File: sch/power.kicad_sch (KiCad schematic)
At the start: 17 parts, among them U6 MAX811MEUS-T

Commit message: Gerber Plots
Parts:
- C1, C14, C5: value (none) -> 10uF; footprint (none) -> Capacitor_SMD:C_0805_2012Metric
- C17, C19, C6: value (none) -> 1uF
- C20, C7, C8: value (none) -> 100nF
- D1: value (none) -> LED; footprint (none) -> LED_SMD:LED_0805_2012Metric
- R29: value (none) -> 4K7; footprint (none) -> Resistor_SMD:R_0805_2012Metric
- REG1: value (none) -> NCP1117ST50T3G; footprint (none) -> Package_TO_SOT_SMD:SOT-223-3_TabPin2
- REG2, REG3: value (none) -> NCP1117ST33T3G; footprint (none) -> Package_TO_SOT_SMD:SOT-223-3_TabPin2
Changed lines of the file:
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@@
       (effects (font (size 1.27 1.27)) hide)
     )
-    (property "Value" "" (id 1) (at 86.995 38.1 0))
+    (property "Value" "GND" (id 1) (at 86.995 38.1 0))
     (property "Footprint" "" (id 2) (at 86.995 33.655 0)
       (effects (font (size 1.27 1.27)) hide)
@@
       (effects (font (size 1.27 1.27)) (justify left))
     )
-    (property "Value" "" (id 1) (at 73.66 63.5 0)
-      (effects (font (size 1.27 1.27)) (justify right))
-    )
-    (property "Footprint" "" (id 2) (at 76.2 62.23 0)
+    (property "Value" "10uF" (id 1) (at 73.66 63.5 0)
+      (effects (font (size 1.27 1.27)) (justify right))
+    )
+    (property "Footprint" "Capacitor_SMD:C_0805_2012Metric" (id 2) (at 76.2 62.23 0)
       (effects (font (size 1.27 1.27)) hide)
     )
@@
       (effects (font (size 1.27 1.27)) (justify left))
     )
-    (property "Value" "" (id 1) (at 73.66 139.7 0)
-      (effects (font (size 1.27 1.27)) (justify right))
-    )
-    (property "Footprint" "" (id 2) (at 76.2 138.43 0)
+    (property "Value" "10uF" (id 1) (at 73.66 139.7 0)
+      (effects (font (size 1.27 1.27)) (justify right))
+    )
+    (property "Footprint" "Capacitor_SMD:C_0805_2012Metric" (id 2) (at 76.2 138.43 0)
       (effects (font (size 1.27 1.27)) hide)
     )
@@
     (in_bom yes) (on_board yes) (fields_autoplaced)
     (property "Reference" "REG1" (id 0) (at 90.17 49.53 0))
-    (property "Value" "" (id 1) (at 90.17 52.07 0))
-    (property "Footprint" "" (id 2) (at 90.17 52.07 0)
+    (property "Value" "NCP1117ST50T3G" (id 1) (at 90.17 52.07 0))
+    (property "Footprint" "Package_TO_SOT_SMD:SOT-223-3_TabPin2" (id 2) (at 90.17 52.07 0)
       (effects (font (size 1.27 1.27)) hide)
     )
@@
     (in_bom yes) (on_board yes) (fields_autoplaced)
     (property "Reference" "REG2" (id 0) (at 90.17 87.63 0))
-    (property "Value" "" (id 1) (at 90.17 90.17 0))
-    (property "Footprint" "" (id 2) (at 90.17 90.17 0)
+    (property "Value" "NCP1117ST33T3G" (id 1) (at 90.17 90.17 0))
+    (property "Footprint" "Package_TO_SOT_SMD:SOT-223-3_TabPin2" (id 2) (at 90.17 90.17 0)
       (effects (font (size 1.27 1.27)) hide)
     )
@@
       (effects (font (size 1.27 1.27)) (justify left))
     )
-    (property "Value" "" (id 1) (at 113.665 101.6 0)
+    (property "Value" "1uF" (id 1) (at 113.665 101.6 0)
       (effects (font (size 1.27 1.27)) (justify right))
     )
@@
       (effects (font (size 1.27 1.27)) (justify left))
     )
-    (property "Value" "" (id 1) (at 123.825 101.6 0)
+    (property "Value" "100nF" (id 1) (at 123.825 101.6 0)
       (effects (font (size 1.27 1.27)) (justify right))
     )
@@
       (effects (font (size 1.27 1.27)) (justify left))
     )
-    (property "Value" "" (id 1) (at 113.665 139.7 0)
+    (property "Value" "1uF" (id 1) (at 113.665 139.7 0)
       (effects (font (size 1.27 1.27)) (justify right))
     )
@@
     (in_bom yes) (on_board yes)
     (property "Reference" "D1" (id 0) (at 71.12 27.305 0))
-    (property "Value" "" (id 1) (at 71.12 29.845 0))
-    (property "Footprint" "" (id 2) (at 71.12 33.655 0)
+    (property "Value" "LED" (id 1) (at 71.12 29.845 0))
+    (property "Footprint" "LED_SMD:LED_0805_2012Metric" (id 2) (at 71.12 33.655 0)
       (effects (font (size 1.27 1.27)) hide)
     )
@@
     (in_bom yes) (on_board yes) (fields_autoplaced)
     (property "Reference" "R29" (id 0) (at 78.74 27.94 90))
-    (property "Value" "" (id 1) (at 78.74 30.48 90))
-    (property "Footprint" "" (id 2) (at 78.74 35.433 90)
+    (property "Value" "4K7" (id 1) (at 78.74 30.48 90))
+    (property "Footprint" "Resistor_SMD:R_0805_2012Metric" (id 2) (at 78.74 35.433 90)
       (effects (font (size 1.27 1.27)) hide)
     )
@@
     (in_bom yes) (on_board yes) (fields_autoplaced)
     (property "Reference" "REG3" (id 0) (at 90.17 125.73 0))
-    (property "Value" "" (id 1) (at 90.17 128.27 0))
-    (property "Footprint" "" (id 2) (at 90.17 128.27 0)
+    (property "Value" "NCP1117ST33T3G" (id 1) (at 90.17 128.27 0))
+    (property "Footprint" "Package_TO_SOT_SMD:SOT-223-3_TabPin2" (id 2) (at 90.17 128.27 0)
       (effects (font (size 1.27 1.27)) hide)
     )
@@
       (effects (font (size 1.27 1.27)) (justify left))
     )
-    (property "Value" "" (id 1) (at 73.66 101.6 0)
-      (effects (font (size 1.27 1.27)) (justify right))
-    )
-    (property "Footprint" "" (id 2) (at 76.2 100.33 0)
+    (property "Value" "10uF" (id 1) (at 73.66 101.6 0)
+      (effects (font (size 1.27 1.27)) (justify right))
+    )
+    (property "Footprint" "Capacitor_SMD:C_0805_2012Metric" (id 2) (at 76.2 100.33 0)
       (effects (font (size 1.27 1.27)) hide)
     )
@@
       (effects (font (size 1.27 1.27)) (justify left))
     )
-    (property "Value" "" (id 1) (at 123.825 63.5 0)
+    (property "Value" "100nF" (id 1) (at 123.825 63.5 0)
       (effects (font (size 1.27 1.27)) (justify right))
     )
@@
       (effects (font (size 1.27 1.27)) (justify left))
     )
-    (property "Value" "" (id 1) (at 123.825 139.7 0)
+    (property "Value" "100nF" (id 1) (at 123.825 139.7 0)
       (effects (font (size 1.27 1.27)) (justify right))
     )
@@
       (effects (font (size 1.27 1.27)) (justify left))
     )
-    (property "Value" "" (id 1) (at 113.665 63.5 0)
-      (effects (font (size 1.27 1.27)) (justify right))
-    )
+    (property "Value" "1uF" (id 1) (at 113.665 63.5 0)
+      (effects (font (size 1.27 1.27)) (justify right))
+    )

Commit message: some docs
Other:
- note added: "Power Delivery"
- note added: "Power Indicator"
- moved on the sheet: C1, C17, C5, C6, C7, C8, REG1, REG2

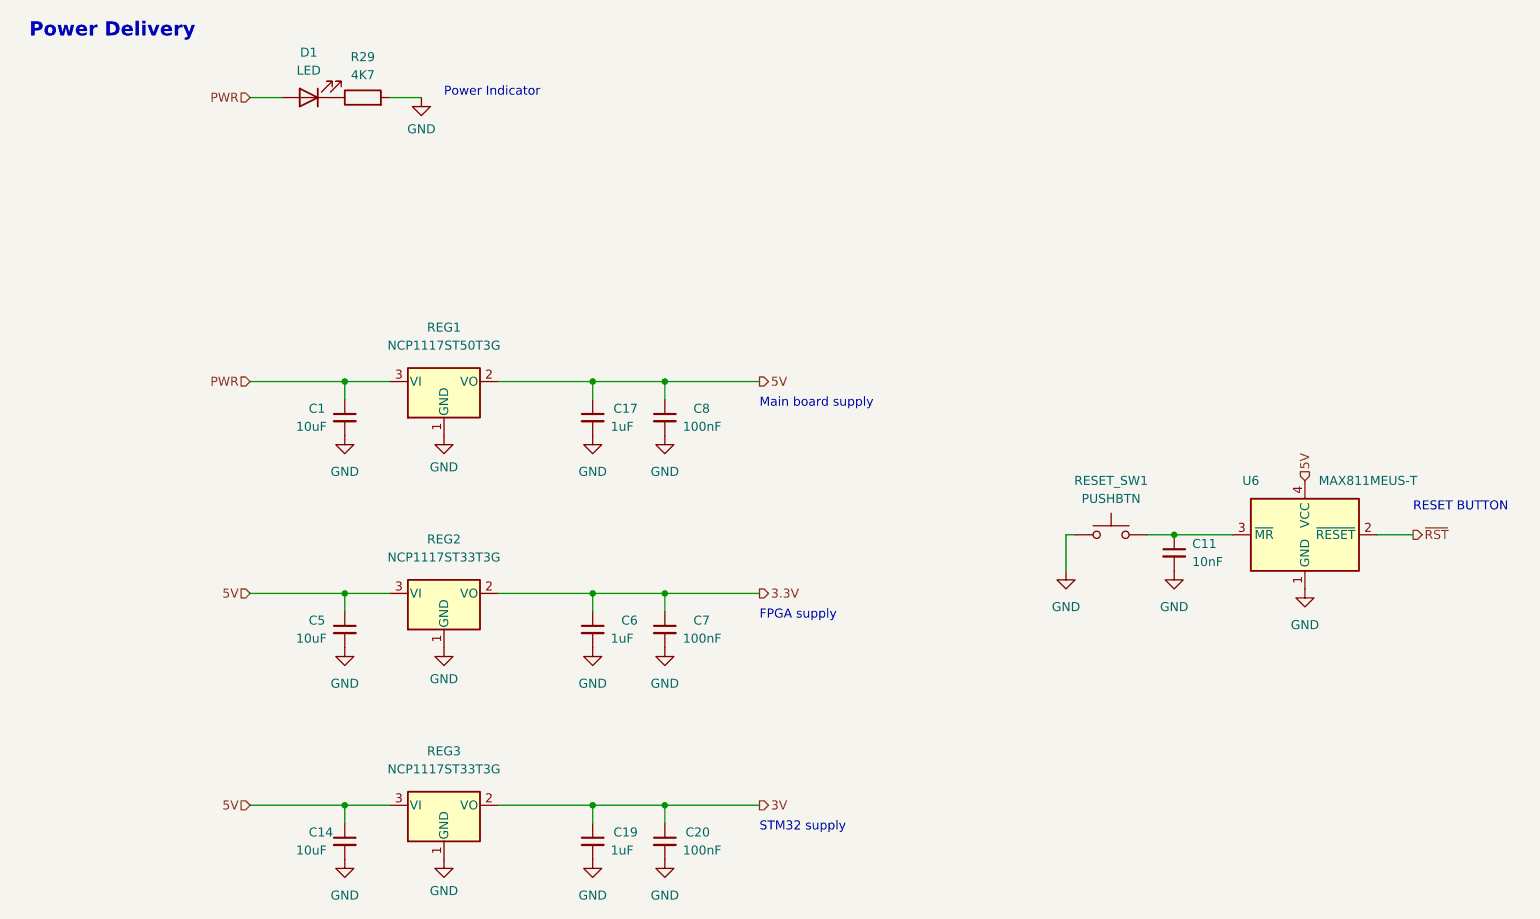
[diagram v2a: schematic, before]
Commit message: update schematic
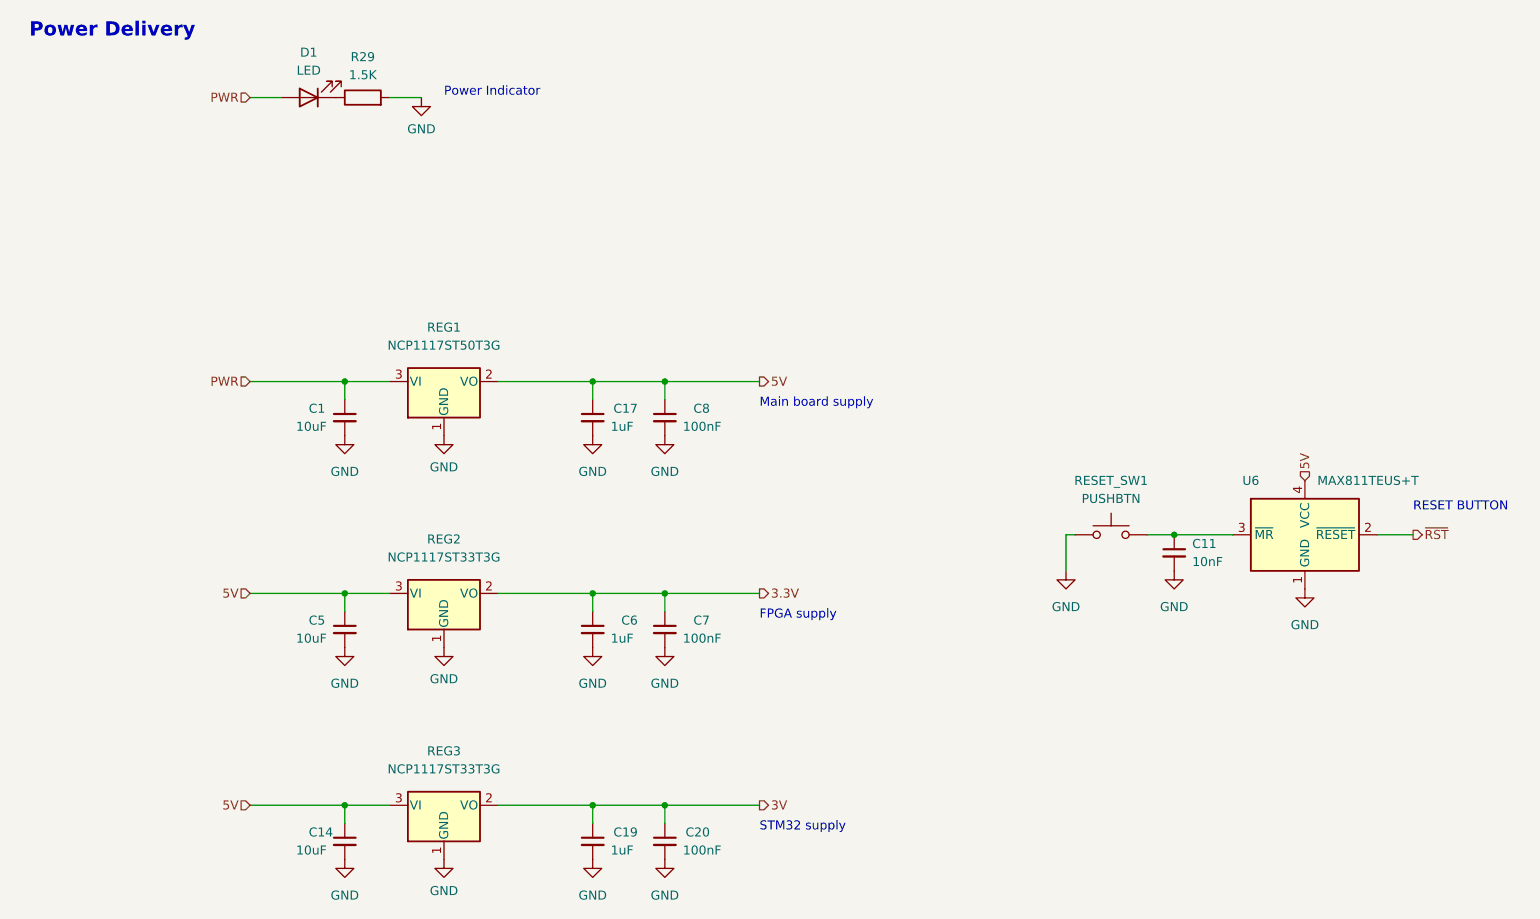
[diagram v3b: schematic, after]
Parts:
- R29: value 4K7 -> 1.5K
- U6: value MAX811MEUS-T -> MAX811TEUS+T
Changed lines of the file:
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@@
     (in_bom yes) (on_board yes) (fields_autoplaced)
     (property "Reference" "R29" (id 0) (at 78.74 27.94 90))
-    (property "Value" "4K7" (id 1) (at 78.74 30.48 90))
+    (property "Value" "1.5K" (id 1) (at 78.74 30.48 90))
     (property "Footprint" "Resistor_SMD:R_0805_2012Metric" (id 2) (at 78.74 35.433 90)
       (effects (font (size 1.27 1.27)) hide)
@@
     (in_bom yes) (on_board yes)
     (property "Reference" "U6" (id 0) (at 203.835 87.63 0))
-    (property "Value" "MAX811MEUS-T" (id 1) (at 220.345 87.63 0))
+    (property "Value" "MAX811TEUS+T" (id 1) (at 220.345 87.63 0))
     (property "Footprint" "Package_TO_SOT_SMD:SOT-143" (id 2) (at 213.995 102.87 0)
       (effects (font (size 1.27 1.27)) (justify left) hide)

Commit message: serial rollback
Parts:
- removed C14: 10uF, Capacitor_SMD:C_0805_2012Metric, symbol Device:C_Small
- removed C19: 1uF, Capacitor_SMD:C_0805_2012Metric, symbol Device:C_Small
- removed C20: 100nF, Capacitor_SMD:C_0805_2012Metric, symbol Device:C_Small
- removed REG3: NCP1117ST33T3G, Package_TO_SOT_SMD:SOT-223-3_TabPin2, symbol Regulator_Linear:NCP1117-5.0_SOT223
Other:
- note removed: "FPGA supply"
- moved on the sheet: C1, C11, C17, C5, C6, C7, C8, D1, R29, REG1, REG2, RESET_SW1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

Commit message: Cleanup board
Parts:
- R29: value 1.5K -> (none)
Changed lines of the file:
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@@
     (in_bom yes) (on_board yes) (fields_autoplaced)
     (property "Reference" "R29" (id 0) (at 52.07 49.53 90))
-    (property "Value" "1.5K" (id 1) (at 52.07 52.07 90))
+    (property "Value" "" (id 1) (at 52.07 52.07 90))
     (property "Footprint" "Resistor_SMD:R_0805_2012Metric" (id 2) (at 52.07 57.023 90)
       (effects (font (size 1.27 1.27)) hide)

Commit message: Clearances
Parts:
- C11: value 10nF -> (none)
- R29: value (none) -> 1K
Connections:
- net 5V: now also D1.2 (A)
- net PWR: no longer D1.2 (A)
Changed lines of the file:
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@@
     (effects (font (size 1.27 1.27)) (justify left))
   )
-  (hierarchical_label "PWR" (shape input) (at 36.195 55.245 180)
+  (hierarchical_label "5V" (shape output) (at 107.95 79.375 0)
+    (effects (font (size 1.27 1.27)) (justify left))
+  )
+  (hierarchical_label "5V" (shape input) (at 36.195 109.22 180)
     (effects (font (size 1.27 1.27)) (justify right))
   )
-  (hierarchical_label "5V" (shape output) (at 107.95 79.375 0)
-    (effects (font (size 1.27 1.27)) (justify left))
-  )
-  (hierarchical_label "5V" (shape input) (at 36.195 109.22 180)
+  (hierarchical_label "5V" (shape input) (at 36.195 55.245 180)
     (effects (font (size 1.27 1.27)) (justify right))
   )
@@
       (effects (font (size 1.27 1.27)) (justify left))
     )
-    (property "Value" "10nF" (id 1) (at 169.545 83.185 0)
+    (property "Value" "" (id 1) (at 169.545 83.185 0)
       (effects (font (size 1.27 1.27)) (justify left))
     )
@@
     (in_bom yes) (on_board yes) (fields_autoplaced)
     (property "Reference" "R29" (id 0) (at 52.07 49.53 90))
-    (property "Value" "" (id 1) (at 52.07 52.07 90))
+    (property "Value" "1K" (id 1) (at 52.07 52.07 90))
     (property "Footprint" "Resistor_SMD:R_0805_2012Metric" (id 2) (at 52.07 57.023 90)
       (effects (font (size 1.27 1.27)) hide)

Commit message: Huge mistake CPU fp
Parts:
- C11: value (none) -> 100nF
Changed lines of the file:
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@@
       (effects (font (size 1.27 1.27)) (justify left))
     )
-    (property "Value" "" (id 1) (at 169.545 83.185 0)
+    (property "Value" "100nF" (id 1) (at 169.545 83.185 0)
       (effects (font (size 1.27 1.27)) (justify left))
     )

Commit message: small updates
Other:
- note added: "Videp MCU supply"
- note removed: "STM32 supply"
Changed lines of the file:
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@@
     (stroke (width 0) (type default) (color 0 0 0 0))
   )
-  (text "RESET BUTTON" (at 200.66 76.2 0)
+  (text "Power Delivery" (at 31.75 25.4 0)
+    (effects (font (size 2 2) (thickness 0.254) bold) (justify left bottom))
+  )
+  (text "RESET BUTTON" (at 200.66 83.82 0)
     (effects (font (size 1.27 1.27)) (justify left bottom))
   )
-  (text "STM32 supply" (at 107.95 113.665 0)
+  (text "Videp MCU supply" (at 107.95 113.665 0)
     (effects (font (size 1.27 1.27)) (justify left bottom))
   )
@@
     (effects (font (size 1.27 1.27)) (justify left bottom))
   )
-  (text "Power Delivery" (at 31.75 25.4 0)
-    (effects (font (size 2 2) (thickness 0.4) bold) (justify left bottom))
-  )
   (text "Main board supply" (at 107.95 83.185 0)
